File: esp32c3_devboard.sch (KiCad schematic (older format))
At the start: 60 parts, among them J1 Micro_USB, J3 Conn_01x15_Male, J4 Conn_01x15_Male, SW1 RST, SW2 BOOT, U1 ESP32-C3-MINI-1, U2 SRV05-4, U3 AMS1117-3.3, U4 CP2102N-A01-GQFN28, U5 USB2514B_Bi, Y1 24MHz

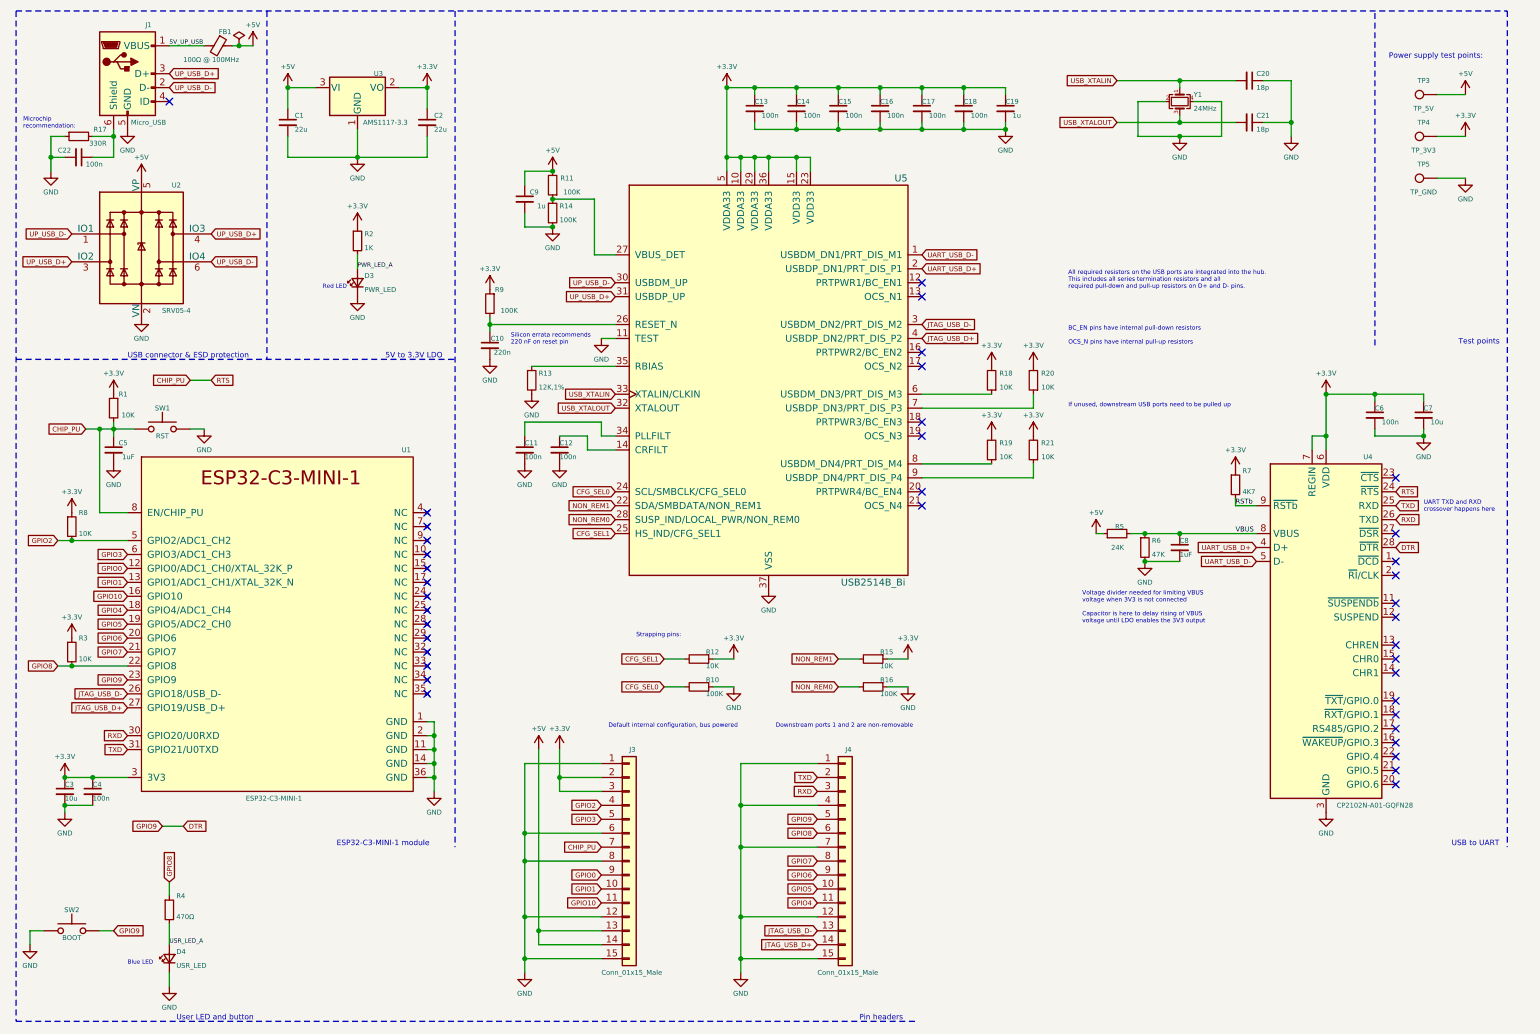
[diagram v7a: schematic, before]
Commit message: Update schematic to be hierarchical
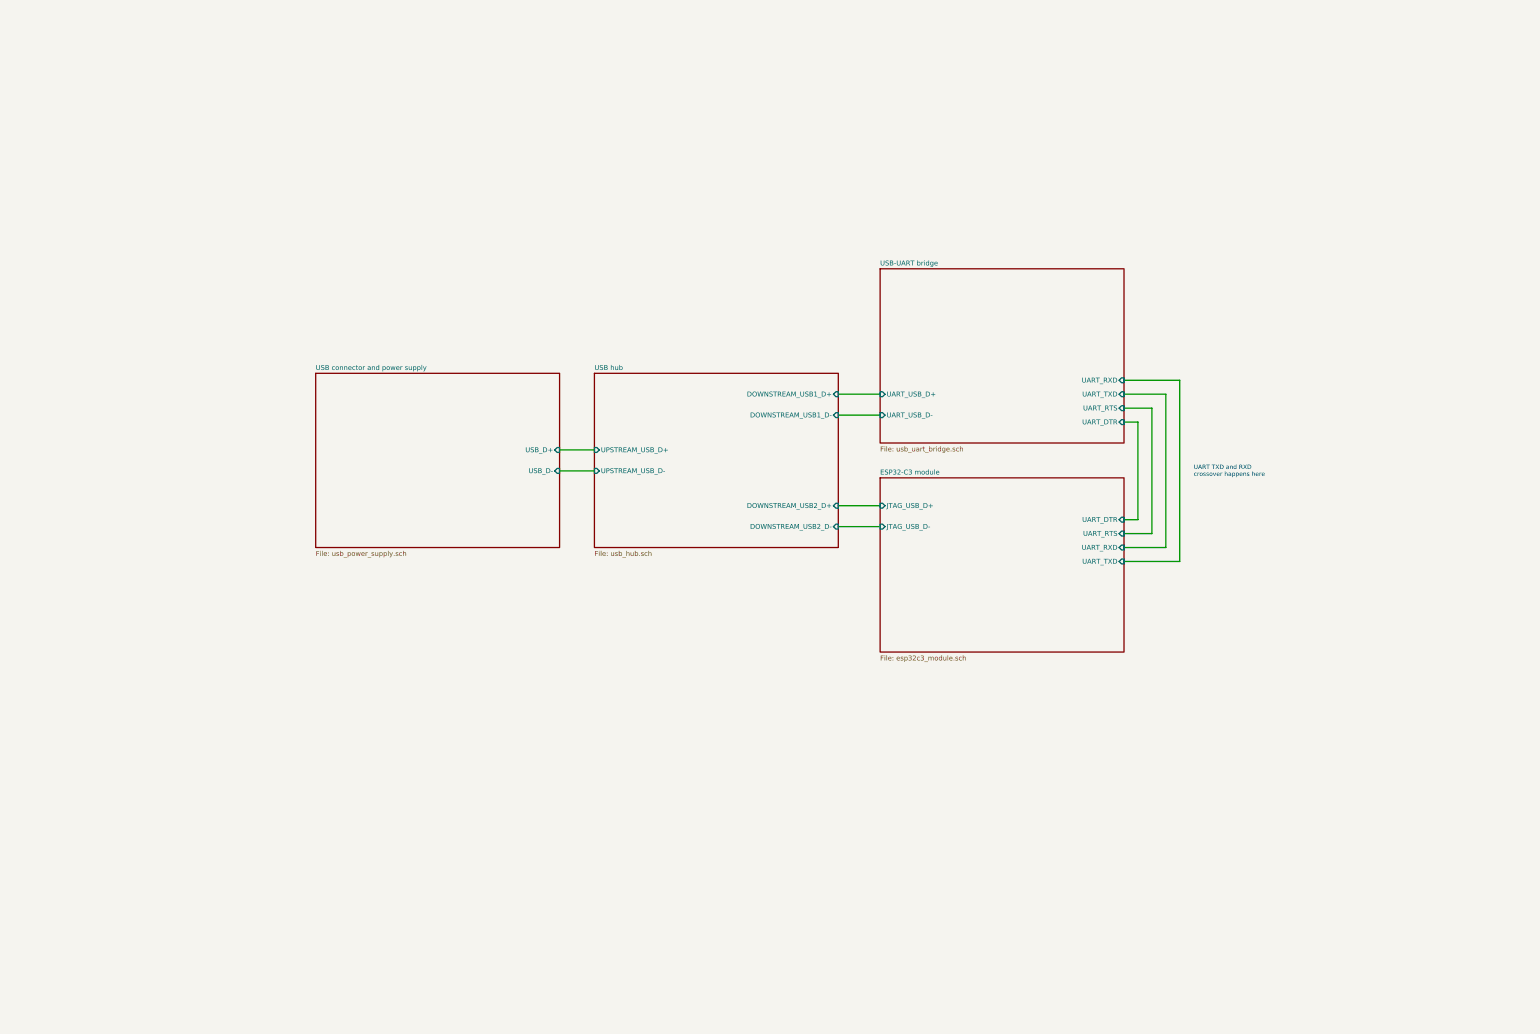
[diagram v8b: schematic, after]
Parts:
- removed C1, C2: 22u, Capacitor_SMD:C_0805_2012Metric, symbol Device:C_Small
- removed C10: 220n, Capacitor_SMD:C_0402_1005Metric, symbol Device:C_Small
- removed C11, C12, C13, C14, C15, C16, C17, C18, C22, C4, C6: 100n, Capacitor_SMD:C_0402_1005Metric, symbol Device:C_Small
- removed C19: 1u, Capacitor_SMD:C_0603_1608Metric, symbol Device:C_Small
- removed C20, C21: 18p, Capacitor_SMD:C_0402_1005Metric, symbol Device:C_Small
- removed C3, C7: 10u, Capacitor_SMD:C_0603_1608Metric, symbol Device:C_Small
- removed C5, C8: 1uF, Capacitor_SMD:C_0402_1005Metric, symbol Device:C_Small
- removed C9: 1u, Capacitor_SMD:C_0402_1005Metric, symbol Device:C_Small
- removed D3: PWR_LED, LED_SMD:LED_0603_1608Metric, symbol Device:LED_Small
- removed D4: USR_LED, LED_SMD:LED_0603_1608Metric, symbol Device:LED_Small
- removed FB1: 100Ω @ 100MHz, Inductor_SMD:L_0805_2012Metric, symbol Device:Ferrite_Bead_Small
- removed J1: Micro_USB, Connector_USB:USB_Micro-B_Wuerth_629105150521, symbol Connector:USB_B_Micro
- removed J3, J4: Conn_01x15_Male, Connector_PinHeader_2.54mm:PinHeader_1x15_P2.54mm_Vertical, symbol Connector_Generic:Conn_01x15
- removed R1, R12, R15, R18, R19, R20, R21, R3, R8: 10K, Resistor_SMD:R_0402_1005Metric, symbol Device:R_Small
- removed R10, R11, R14, R16, R9: 100K, Resistor_SMD:R_0402_1005Metric, symbol Device:R_Small
- removed R13: 12K,1%, Resistor_SMD:R_0402_1005Metric, symbol Device:R_Small
- removed R17: 330R, Resistor_SMD:R_0402_1005Metric, symbol Device:R_Small
- removed R2: 1K, Resistor_SMD:R_0603_1608Metric, symbol Device:R_Small
- removed R4: 470Ω, Resistor_SMD:R_0603_1608Metric, symbol Device:R_Small
- removed R5: 24K, Resistor_SMD:R_0402_1005Metric, symbol Device:R_Small
- removed R6: 47K, Resistor_SMD:R_0402_1005Metric, symbol Device:R_Small
- removed R7: 4K7, Resistor_SMD:R_0402_1005Metric, symbol Device:R_Small
- removed SW1: RST, Button_Switch_SMD:SW_SPST_TL3342, symbol Switch:SW_Push
- removed SW2: BOOT, Button_Switch_SMD:SW_SPST_TL3342, symbol Switch:SW_Push
- removed TP3: TP_5V, TestPoint:TestPoint_Pad_D1.0mm, symbol Connector:TestPoint
- removed TP4: TP_3V3, TestPoint:TestPoint_Pad_D1.0mm, symbol Connector:TestPoint
- removed TP5: TP_GND, TestPoint:TestPoint_Pad_D1.0mm, symbol Connector:TestPoint
- removed U1: ESP32-C3-MINI-1, Espressif:ESP32-C3-MINI-1, symbol Espressif:ESP32-C3-MINI-1
- removed U2: SRV05-4, Package_TO_SOT_SMD:SOT-23-6, symbol Power_Protection:SRV05-4
- removed U3: AMS1117-3.3, Package_TO_SOT_SMD:SOT-223-3_TabPin2, symbol Regulator_Linear:AMS1117-3.3
- removed U4: CP2102N-A01-GQFN28, Package_DFN_QFN:QFN-28-1EP_5x5mm_P0.5mm_EP3.35x3.35mm, symbol Interface_USB:CP2102N-A01-GQFN28
- removed U5: USB2514B_Bi, Package_DFN_QFN:QFN-36-1EP_6x6mm_P0.5mm_EP3.7x3.7mm, symbol Interface_USB:USB2514B_Bi
- removed Y1: 24MHz, Crystal:Crystal_SMD_2016-4Pin_2.0x1.6mm, symbol Device:Crystal_GND24_Small
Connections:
- no-connect marks 39 -> 0
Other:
- note removed: "5V to 3.3V LDO"
- note removed: "All required resistors on the USB ports are integrated into the hub.\nThis includes all series termination resistors and all\nrequired pull-down and pull-up resistors on D+ and D- pins."
- note removed: "BC_EN pins have internal pull-down resistors"
- note removed: "Blue LED"
- note removed: "Default internal configuration, bus powered"
- note removed: "Downstream ports 1 and 2 are non-removable"
- note removed: "ESP32-C3-MINI-1 module"
- note removed: "If unused, downstream USB ports need to be pulled up"
- note removed: "Microchip\nrecommendation:"
- note removed: "OCS_N pins have internal pull-up resistors"
- note removed: "Pin headers"
- note removed: "Power supply test points:"
- note removed: "Red LED"
- note removed: "Silicon errata recommends\n220 nF on reset pin"
- note removed: "Strapping pins:"
- note removed: "Test points"
- note removed: "USB connector & ESD protection"
- note removed: "USB to UART"
- note removed: "User LED and button"
- note removed: "Voltage divider needed for limiting VBUS\nvoltage when 3V3 is not connected\n\nCapacitor is here to delay rising of VBUS\nvoltage until LDO enables the 3V3 output"
